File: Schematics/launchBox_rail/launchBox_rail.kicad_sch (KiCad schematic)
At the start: 13 parts, among them J1 Screw_Terminal_01x02, J2 Screw_Terminal_01x02, Q1 NMOS, SW1 SW_MEC_5G

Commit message: Updated component layouts for LPB
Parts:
- J1, J2: footprint (none) -> Connector_PinHeader_1.00mm:PinHeader_1x02_P1.00mm_Vertical
- R1, R2, R3, R4, R5, R6, R7: footprint (none) -> Resistor_SMD:R_0603_1608Metric

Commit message: Updated PCB for LPB 80% done
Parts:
- removed A1: Arduino_UNO_R3, Module:Arduino_UNO_R3, symbol MCU_Module:Arduino_UNO_R3
- added A2: Arduino_Nano_v3.x, Module:Arduino_Nano, symbol MCU_Module:Arduino_Nano_v3.x
- added J3: RadioConnectorRxTx, Connector_PinHeader_1.00mm:PinHeader_1x02_P1.00mm_Vertical, symbol Connector:Conn_01x02_Pin
- added J4: RadioConnectorPWR, Connector_PinHeader_1.00mm:PinHeader_1x02_P1.00mm_Vertical, symbol Connector:Conn_01x02_Pin
- BZ1: footprint (none) -> Connector_PinHeader_1.00mm:PinHeader_1x02_P1.00mm_Vertical
- J1: footprint Connector_PinHeader_1.00mm:PinHeader_1x02_P1.00mm_Vertical -> Connector_PinHeader_1.00mm:PinHeader_1x03_P1.00mm_Vertical
- Q1, SW1: footprint (none) -> Connector_PinHeader_1.00mm:PinHeader_1x03_P1.00mm_Vertical
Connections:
- net +12V: now also A2.30 (VIN)
- net GNDREF: now also A2.29 (GND), A2.4 (GND), J4.2 (Pin_2)
- net trigger: now also A2.5 (D2)
- net at R6.2, R7.1: now also A2.23 (A4)
- net at R5.2: now also A2.9 (D6)
- new net: A2.1 (D1/TX), J3.2 (Pin_2)
- new net: A2.2 (D0/RX), J3.1 (Pin_1)
- new net radioPWR: A2.27 (+5V), J4.1 (Pin_1)

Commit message: v1 of PCB for LPB is complete
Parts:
- removed J3: RadioConnectorRxTx, Connector_PinHeader_1.00mm:PinHeader_1x02_P1.00mm_Vertical, symbol Connector:Conn_01x02_Pin
- removed J4: RadioConnectorPWR, Connector_PinHeader_1.00mm:PinHeader_1x02_P1.00mm_Vertical, symbol Connector:Conn_01x02_Pin
- added J5: Conn_01x04_Pin, Connector_PinHeader_2.54mm:PinHeader_1x04_P2.54mm_Vertical, symbol Connector:Conn_01x04_Pin
- BZ1, J2: footprint Connector_PinHeader_1.00mm:PinHeader_1x02_P1.00mm_Vertical -> Connector_PinHeader_2.54mm:PinHeader_1x02_P2.54mm_Vertical
- J1, SW1: footprint Connector_PinHeader_1.00mm:PinHeader_1x03_P1.00mm_Vertical -> Connector_PinHeader_2.54mm:PinHeader_1x02_P2.54mm_Vertical
- Q1: footprint Connector_PinHeader_1.00mm:PinHeader_1x03_P1.00mm_Vertical -> Connector_PinHeader_2.54mm:PinHeader_1x03_P2.54mm_Vertical
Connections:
- net GNDREF: now also J5.2 (Pin_2)
- net continuity: now also A2.26 (A7)
- net radioPWR: now also J5.1 (Pin_1)
- net radioTx: now reaches A2.1 (D1/TX)
- net radioTx: now also J5.3 (Pin_3)
- net radioRx: now reaches A2.2 (D0/RX)
- net radioRx: now also J5.4 (Pin_4)
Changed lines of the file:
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@@
+	(wire
+		(pts
+			(xy 50.8 55.88) (xy 27.94 55.88)
+		)
+		(stroke
+			(width 0)
+			(type default)
+		)
+	)
 	(wire
 		(pts
@@
 	(wire
 		(pts
+			(xy 50.8 52.07) (xy 50.8 55.88)
+		)
+		(stroke
+			(width 0)
+			(type default)
+		)
+	)
+	(wire
+		(pts
 			(xy 74.93 104.14) (xy 74.93 110.49)
 		)
@@
 	(wire
 		(pts
+			(xy 53.34 54.61) (xy 53.34 58.42)
+		)
+		(stroke
+			(width 0)
+			(type default)
+		)
+	)
+	(wire
+		(pts
 			(xy 133.35 62.23) (xy 142.24 62.23)
 		)
@@
 	(wire
 		(pts
-			(xy 62.23 52.07) (xy 53.34 52.07)
+			(xy 50.8 52.07) (xy 62.23 52.07)
 		)
 		(stroke
@@
 	(wire
 		(pts
+			(xy 54.61 63.5) (xy 62.23 63.5)
+		)
+		(stroke
+			(width 0)
+			(type default)
+		)
+	)
+	(wire
+		(pts
 			(xy 170.18 73.66) (xy 170.18 78.74)
 		)
@@
 	(wire
 		(pts
+			(xy 35.56 60.96) (xy 27.94 60.96)
+		)
+		(stroke
+			(width 0)
+			(type default)
+		)
+	)
+	(wire
+		(pts
 			(xy 119.38 59.69) (xy 119.38 62.23)
 		)
@@
 	(wire
 		(pts
-			(xy 53.34 64.77) (xy 62.23 64.77)
+			(xy 35.56 63.5) (xy 27.94 63.5)
 		)
 		(stroke
@@
 	(wire
 		(pts
-			(xy 62.23 62.23) (xy 62.23 63.5)
+			(xy 53.34 58.42) (xy 27.94 58.42)
 		)
 		(stroke
@@
 	(wire
 		(pts
+			(xy 87.63 96.52) (xy 99.06 96.52)
+		)
+		(stroke
+			(width 0)
+			(type default)
+		)
+	)
+	(wire
+		(pts
 			(xy 128.27 74.93) (xy 137.16 74.93)
 		)
@@
 	(wire
 		(pts
-			(xy 62.23 64.77) (xy 62.23 66.04)
-		)
-		(stroke
-			(width 0)
-			(type default)
-		)
-	)
-	(wire
-		(pts
 			(xy 87.63 88.9) (xy 105.41 88.9)
 		)
@@
 	(wire
 		(pts
-			(xy 53.34 62.23) (xy 62.23 62.23)
-		)
-		(stroke
-			(width 0)
-			(type default)
-		)
-	)
-	(wire
-		(pts
 			(xy 142.24 78.74) (xy 142.24 81.28)
 		)
@@
 	(wire
 		(pts
+			(xy 54.61 66.04) (xy 62.23 66.04)
+		)
+		(stroke
+			(width 0)
+			(type default)
+		)
+	)
+	(wire
+		(pts
 			(xy 153.67 43.18) (xy 153.67 29.21)
 		)
@@
 		)
 	)
+	(label "radioRx"
+		(at 35.56 63.5 180)
+		(effects
+			(font
+				(size 1.27 1.27)
+			)
+			(justify right bottom)
+		)
+	)
 	(label "continuity"
-		(at 87.63 99.06 0)
+		(at 99.06 96.52 180)
+		(effects
+			(font
+				(size 1.27 1.27)
+			)
+			(justify right bottom)
+		)
+	)
+	(label "radioTx"
+		(at 35.56 60.96 180)
+		(effects
+			(font
+				(size 1.27 1.27)
+			)
+			(justify right bottom)
+		)
+	)
+	(label "radioRx"
+		(at 54.61 63.5 0)
 		(effects
 			(font
@@
 		)
 	)
+	(label "radioTx"
+		(at 54.61 66.04 0)
+		(effects
+			(font
+				(size 1.27 1.27)
+			)
+			(justify left bottom)
+		)
+	)
 	(label "radioGND"
 		(at 139.7 110.49 180)
@@
 			)
 		)
-		(property "Footprint" "Connector_PinHeader_1.00mm:PinHeader_1x03_P1.00mm_Vertical"
+		(property "Footprint" "Connector_PinHeader_2.54mm:PinHeader_1x02_P2.54mm_Vertical"
 			(at 194.31 62.23 0)
 			(effects
@@
 			)
 		)
-		(property "Footprint" "Connector_PinHeader_1.00mm:PinHeader_1x03_P1.00mm_Vertical"
+		(property "Footprint" "Connector_PinHeader_2.54mm:PinHeader_1x02_P2.54mm_Vertical"
 			(at 128.27 57.15 0)
 			(effects
@@
 			)
 		)
-		(property "Footprint" "Connector_PinHeader_1.00mm:PinHeader_1x03_P1.00mm_Vertical"
+		(property "Footprint" "Connector_PinHeader_2.54mm:PinHeader_1x03_P2.54mm_Vertical"
 			(at 160.02 76.2 0)
 			(effects
@@
 			)
 		)
-		(property "Footprint" "Connector_PinHeader_1.00mm:PinHeader_1x02_P1.00mm_Vertical"
+		(property "Footprint" "Connector_PinHeader_2.54mm:PinHeader_1x02_P2.54mm_Vertical"
 			(at 50.165 83.82 90)
 			(effects
@@
 	)
 	(symbol
-		(lib_id "Connector:Conn_01x02_Pin")
-		(at 48.26 52.07 0)
-		(unit 1)
-		(exclude_from_sim no)
-		(in_bom yes)
-		(on_board yes)
-		(dnp no)
-		(property "Reference" "J4"
-			(at 47.6249 50.8 0)
-			(effects
-				(font
-					(size 1.27 1.27)
-				)
-				(justify left)
-			)
-		)
-		(property "Value" "RadioConnectorPWR"
-			(at 47.498 48.768 0)
-			(effects
-				(font
-					(size 1.27 1.27)
-				)
-				(justify left)
-			)
-		)
-		(property "Footprint" "Connector_PinHeader_1.00mm:PinHeader_1x02_P1.00mm_Vertical"
-			(at 48.26 52.07 0)
-			(effects
-				(font
-					(size 1.27 1.27)
-				)
-				(hide yes)
-			)
-		)
-		(property "Datasheet" "~"
-			(at 48.26 52.07 0)
-			(effects
-				(font
-					(size 1.27 1.27)
-				)
-				(hide yes)
-			)
-		)
-		(property "Description" "Generic connector, single row, 01x02, script generated"
-			(at 48.26 52.07 0)
-			(effects
-				(font
-					(size 1.27 1.27)
-				)
-				(hide yes)
-			)
-		)
-		(pin "1"
-		)
-		(pin "2"
-		)
-		(instances
-			(project "launchBox_rail"
-				(path "/3572cdd5-e58b-4971-9298-7fa35d6d272d"
-					(reference "J4")
-					(unit 1)
-				)
-			)
-		)
-	)
-	(symbol
 		(lib_id "Connector:Screw_Terminal_01x02")
 		(at 194.31 41.91 0)
@@
 			)
 		)
-		(property "Footprint" "Connector_PinHeader_1.00mm:PinHeader_1x02_P1.00mm_Vertical"
+		(property "Footprint" "Connector_PinHeader_2.54mm:PinHeader_1x02_P2.54mm_Vertical"
 			(at 194.31 41.91 0)
 			(effects
@@
 	)
 	(symbol
-		(lib_id "Connector:Conn_01x02_Pin")
-		(at 48.26 62.23 0)
-		(unit 1)
-		(exclude_from_sim no)
-		(in_bom yes)
-		(on_board yes)
-		(dnp no)
-		(fields_autoplaced yes)
-		(property "Reference" "J3"
-			(at 48.895 57.15 0)
-			(effects
-				(font
-					(size 1.27 1.27)
-				)
-			)
-		)
-		(property "Value" "RadioConnectorRxTx"
-			(at 48.895 59.69 0)
-			(effects
-				(font
-					(size 1.27 1.27)
-				)
-			)
-		)
-		(property "Footprint" "Connector_PinHeader_1.00mm:PinHeader_1x02_P1.00mm_Vertical"
-			(at 48.26 62.23 0)
+		(lib_id "Connector:Conn_01x04_Pin")
+		(at 22.86 58.42 0)
+		(unit 1)
+		(exclude_from_sim no)
+		(in_bom yes)
+		(on_board yes)
+		(dnp no)
+		(fields_autoplaced yes)
+		(property "Reference" "J5"
+			(at 23.495 50.8 0)
+			(effects
+				(font
+					(size 1.27 1.27)
+				)
+			)
+		)
+		(property "Value" "Conn_01x04_Pin"
+			(at 23.495 53.34 0)
+			(effects
+				(font
+					(size 1.27 1.27)
+				)
+			)
+		)
+		(property "Footprint" "Connector_PinHeader_2.54mm:PinHeader_1x04_P2.54mm_Vertical"
+			(at 22.86 58.42 0)
 			(effects
 				(font
@@
 		)
 		(property "Datasheet" "~"
-			(at 48.26 62.23 0)
-			(effects
-				(font
-					(size 1.27 1.27)
-				)
-				(hide yes)
-			)
-		)
-		(property "Description" "Generic connector, single row, 01x02, script generated"
-			(at 48.26 62.23 0)
+			(at 22.86 58.42 0)
+			(effects
+				(font
+					(size 1.27 1.27)
+				)
+				(hide yes)
+			)
+		)
+		(property "Description" "Generic connector, single row, 01x04, script generated"
+			(at 22.86 58.42 0)
 			(effects
 				(font
@@
 		(pin "2"
 		)
+		(pin "3"
+		)
+		(pin "4"
+		)
 		(instances
 			(project ""
 				(path "/3572cdd5-e58b-4971-9298-7fa35d6d272d"
-					(reference "J3")
-					(unit 1)
-				)
+					(reference "J5")
+					(unit 1)
+				)

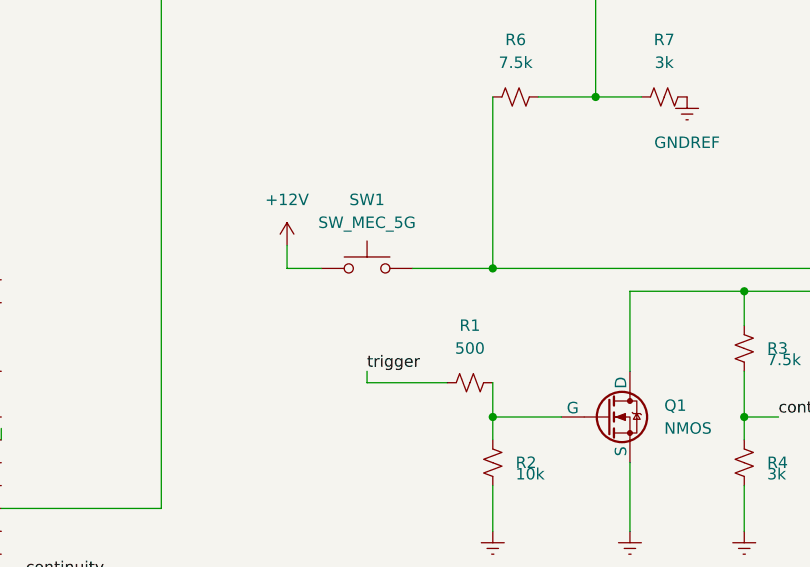
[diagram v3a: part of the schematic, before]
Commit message: Finished LPB PCB design
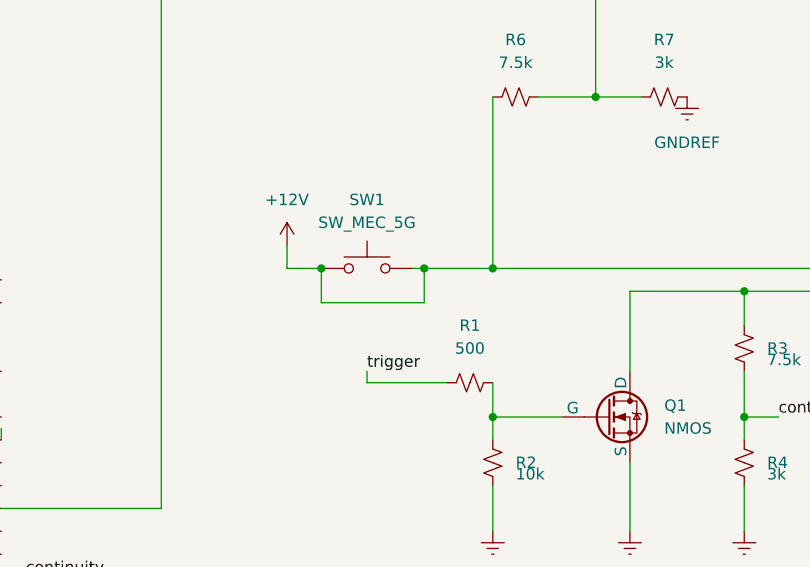
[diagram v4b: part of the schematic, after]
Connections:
- net +12V: now also J1.1 (Pin_1), R6.1, SW1.3 (B), SW1.4 (B)
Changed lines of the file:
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@@
 	(paper "A3")
 	(junction
+		(at 134.62 62.23)
+		(diameter 0)
+		(color 0 0 0 0)
+	)
+	(junction
 		(at 142.24 78.74)
 		(diameter 0)
@@
 	)
 	(junction
+		(at 123.19 62.23)
+		(diameter 0)
+		(color 0 0 0 0)
+	)
+	(junction
 		(at 170.18 78.74)
 		(diameter 0)
@@
 	(wire
 		(pts
-			(xy 133.35 62.23) (xy 142.24 62.23)
+			(xy 133.35 62.23) (xy 134.62 62.23)
 		)
 		(stroke
@@
 	(wire
 		(pts
+			(xy 134.62 62.23) (xy 142.24 62.23)
+		)
+		(stroke
+			(width 0)
+			(type default)
+		)
+	)
+	(wire
+		(pts
 			(xy 72.39 48.26) (xy 72.39 53.34)
 		)
@@
 	(wire
 		(pts
+			(xy 123.19 66.04) (xy 134.62 66.04)
+		)
+		(stroke
+			(width 0)
+			(type default)
+		)
+	)
+	(wire
+		(pts
 			(xy 142.24 43.18) (xy 142.24 62.23)
 		)
@@
 	(wire
 		(pts
+			(xy 123.19 62.23) (xy 123.19 66.04)
+		)
+		(stroke
+			(width 0)
+			(type default)
+		)
+	)
+	(wire
+		(pts
 			(xy 35.56 63.5) (xy 27.94 63.5)
 		)
@@
 		)
 		(stroke
+			(width 0)
+			(type default)
+		)
+	)
+	(wire
+		(pts
+			(xy 134.62 66.04) (xy 134.62 62.23)
+		)
+		(stroke

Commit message: Fixed short
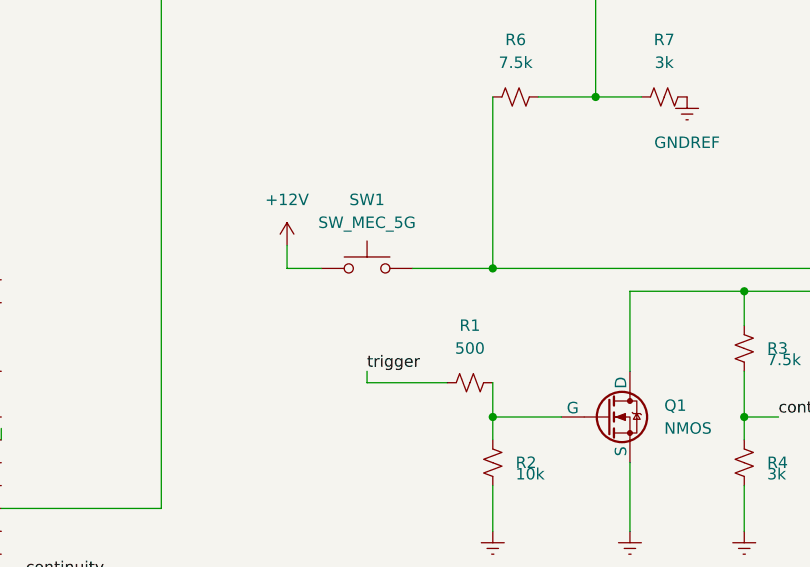
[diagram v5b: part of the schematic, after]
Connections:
- net +12V: no longer J1.1 (Pin_1), R6.1, SW1.3 (B), SW1.4 (B)
- new net: J1.1 (Pin_1), R6.1, SW1.3 (B), SW1.4 (B)
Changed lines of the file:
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@@
 	(paper "A3")
 	(junction
-		(at 134.62 62.23)
-		(diameter 0)
-		(color 0 0 0 0)
-	)
-	(junction
 		(at 142.24 78.74)
 		(diameter 0)
@@
 	)
 	(junction
-		(at 123.19 62.23)
-		(diameter 0)
-		(color 0 0 0 0)
-	)
-	(junction
 		(at 170.18 78.74)
 		(diameter 0)
@@
 	(wire
 		(pts
-			(xy 133.35 62.23) (xy 134.62 62.23)
-		)
-		(stroke
-			(width 0)
-			(type default)
-		)
-	)
-	(wire
-		(pts
 			(xy 62.23 54.61) (xy 53.34 54.61)
 		)
@@
 	(wire
 		(pts
-			(xy 134.62 62.23) (xy 142.24 62.23)
+			(xy 133.35 62.23) (xy 142.24 62.23)
 		)
 		(stroke
@@
 	(wire
 		(pts
-			(xy 123.19 66.04) (xy 134.62 66.04)
-		)
-		(stroke
-			(width 0)
-			(type default)
-		)
-	)
-	(wire
-		(pts
 			(xy 142.24 43.18) (xy 142.24 62.23)
 		)
@@
 	(wire
 		(pts
-			(xy 123.19 62.23) (xy 123.19 66.04)
-		)
-		(stroke
-			(width 0)
-			(type default)
-		)
-	)
-	(wire
-		(pts
 			(xy 35.56 63.5) (xy 27.94 63.5)
 		)
@@
 		)
 		(stroke
-			(width 0)
-			(type default)
-		)
-	)
-	(wire
-		(pts
-			(xy 134.62 66.04) (xy 134.62 62.23)
-		)
-		(stroke

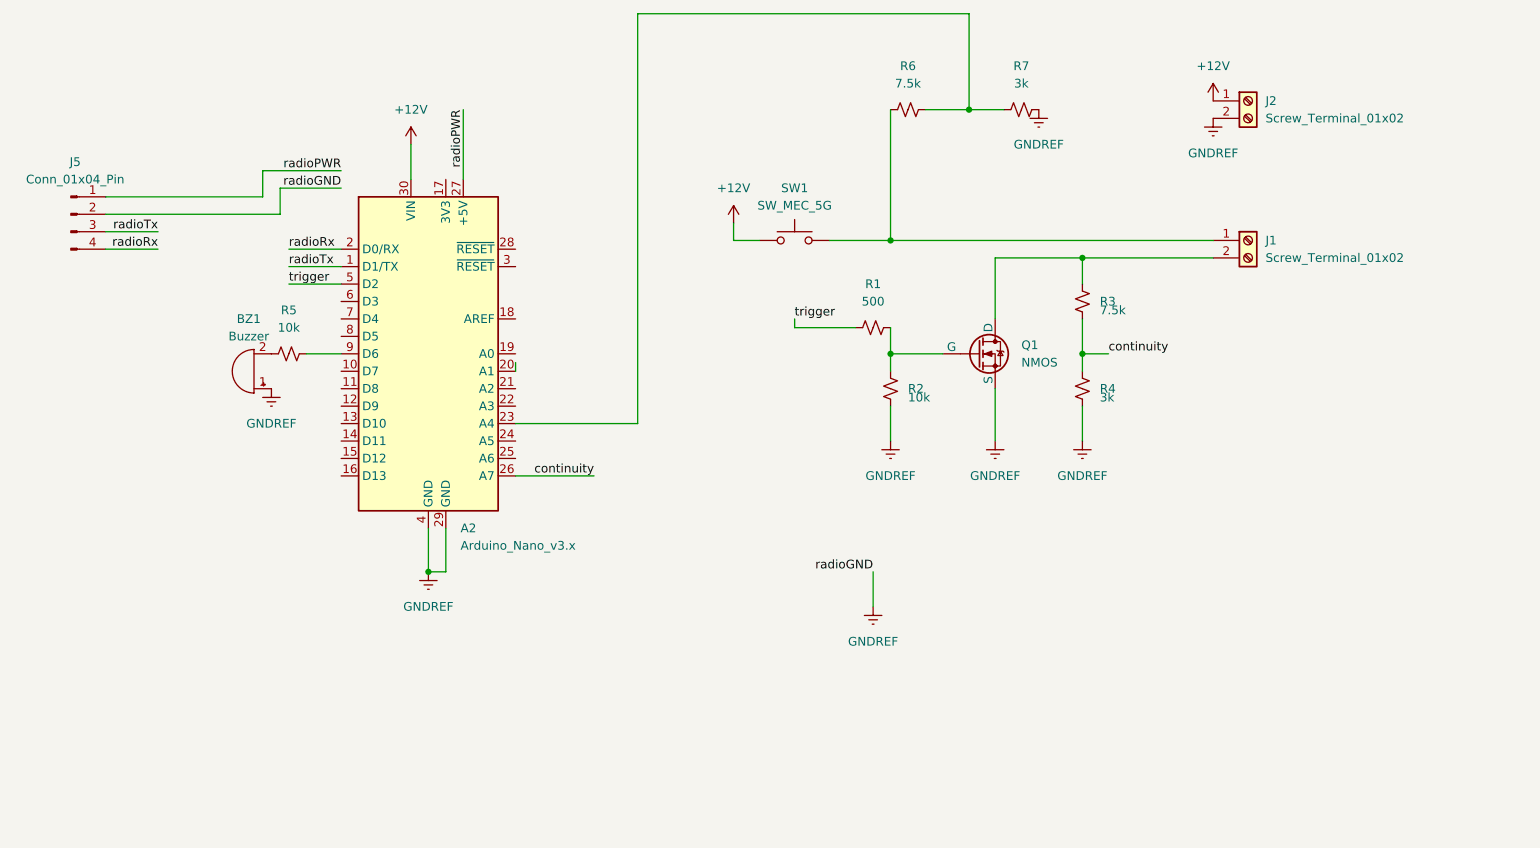
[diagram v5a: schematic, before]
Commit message: Cleaned up rail side launch box schematic and PCB
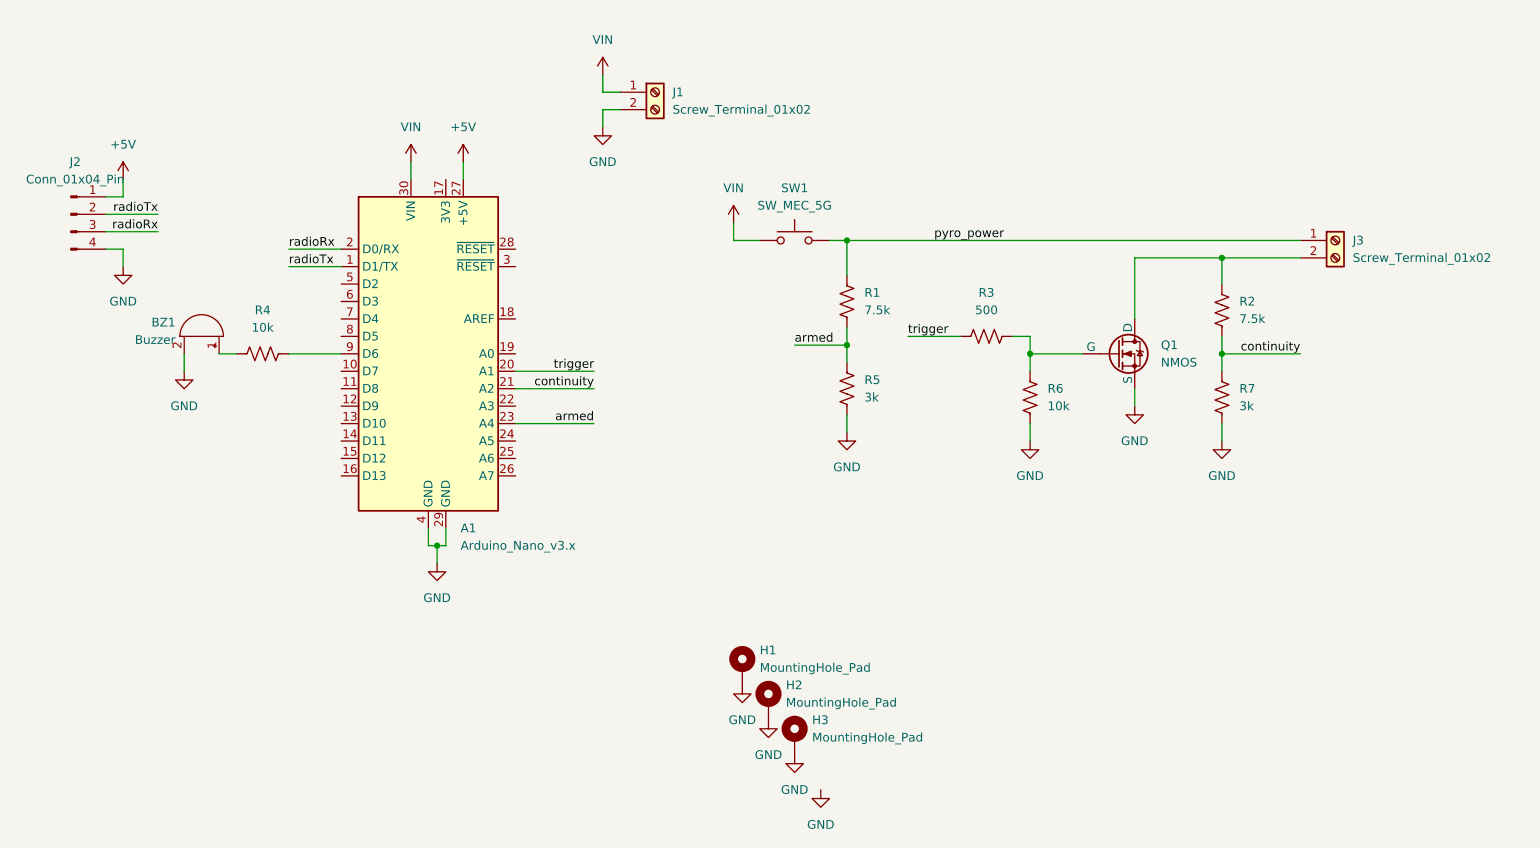
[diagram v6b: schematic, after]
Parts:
- removed R1: 500, Resistor_SMD:R_0603_1608Metric, symbol Device:R_Small_US
- removed R2, R5: 10k, Resistor_SMD:R_0603_1608Metric, symbol Device:R_Small_US
- removed R3, R6: 7.5k, Resistor_SMD:R_0603_1608Metric, symbol Device:R_Small_US
- removed R4, R7: 3k, Resistor_SMD:R_0603_1608Metric, symbol Device:R_Small_US
- added H1, H2, H3: MountingHole_Pad, MountingHole:MountingHole_3.2mm_M3_Pad_TopBottom, symbol Mechanical:MountingHole_Pad
- added R1, R2: 7.5k, Resistor_SMD:R_0603_1608Metric_Pad0.98x0.95mm_HandSolder, symbol Device:R_US
- added R3: 500, Resistor_SMD:R_0603_1608Metric, symbol Device:R_US
- added R4: 10k, Resistor_SMD:R_0603_1608Metric, symbol Device:R_US
- added R5, R7: 3k, Resistor_SMD:R_0603_1608Metric_Pad0.98x0.95mm_HandSolder, symbol Device:R_US
- added R6: 10k, Resistor_SMD:R_0603_1608Metric_Pad0.98x0.95mm_HandSolder, symbol Device:R_US
- renumbered A2 to A1, J2 to J1, J5 to J2, J1 to J3
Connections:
- net continuity: now also A1.21 (A2), R2.2, R7.1; no longer A1.26 (A7)
- net radioRx: now also J2.3 (Pin_3); no longer J2.4 (Pin_4)
- net radioTx: now also J2.2 (Pin_2); no longer J2.3 (Pin_3)
- net trigger: now also A1.20 (A1), R3.1; no longer A1.5 (D2)
- net pyro_power: now reaches J3.1 (Pin_1), SW1.4 (B)
- net pyro_power: now also SW1.2 (A), R1.1; no longer SW1.3 (B)
- net at J3.2 (Pin_2), Q1.1 (D): now also R2.1
- net armed: now reaches A1.23 (A4)
- net armed: now also R1.2, R5.1
- net at Q1.2 (G): now also R3.2, R6.1
- net at A1.9 (D6): now also R4.2
- net GND: now reaches BZ1.2 (+)
- net GND: now also A1.29 (GND), A1.4 (GND), J1.2 (Pin_2), J2.4 (Pin_4), Q1.3 (S), H1.1, H2.1, H3.1, R5.2, R6.2, R7.2
- net +12V renamed VIN
- removed net GNDREF: A1.29 (GND), A1.4 (GND), BZ1.1 (-), J1.2 (Pin_2), J2.2 (Pin_2), Q1.3 (S)
- net radioPWR renamed +5V
- new net: BZ1.1 (-), R4.1
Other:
- moved on the sheet: BZ1, J1, J3, Q1

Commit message: Clean it up a bit more
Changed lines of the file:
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@@
-		(lib_name "GND_1")
-		(lib_id "power:GND")
-		(at 132.08 142.24 0)
-		(unit 1)
-		(exclude_from_sim no)
-		(in_bom yes)
-		(on_board yes)
-		(dnp no)
-		(fields_autoplaced yes)
-		(property "Reference" "#PWR017"
-			(at 132.08 148.59 0)
-			(effects
-				(font
-					(size 1.27 1.27)
-				)
-				(hide yes)
-			)
-		)
-		(property "Value" "GND"
-			(at 132.08 147.32 0)
-			(effects
-				(font
-					(size 1.27 1.27)
-				)
-			)
-		)
-		(property "Footprint" ""
-			(at 132.08 142.24 0)
-			(effects
-				(font
-					(size 1.27 1.27)
-				)
-				(hide yes)
-			)
-		)
-		(property "Datasheet" ""
-			(at 132.08 142.24 0)
-			(effects
-				(font
-					(size 1.27 1.27)
-				)
-				(hide yes)
-			)
-		)
-		(property "Description" "Power symbol creates a global label with name \"GND\" , ground"
-			(at 132.08 142.24 0)
-			(effects
-				(font
-					(size 1.27 1.27)
-				)
-				(hide yes)
-			)
-		)
-		(pin "1"
-		)
-		(instances
-			(project "launchBox_rail"
-				(path "/3572cdd5-e58b-4971-9298-7fa35d6d272d"
-					(reference "#PWR017")
-					(unit 1)
-				)
-			)
-		)
-	)
-	(symbol
 		(lib_name "GND_1")
 		(lib_id "power:GND")
